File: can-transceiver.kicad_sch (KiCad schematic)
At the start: 4 parts, among them U600 TJA1044GTK_3Z

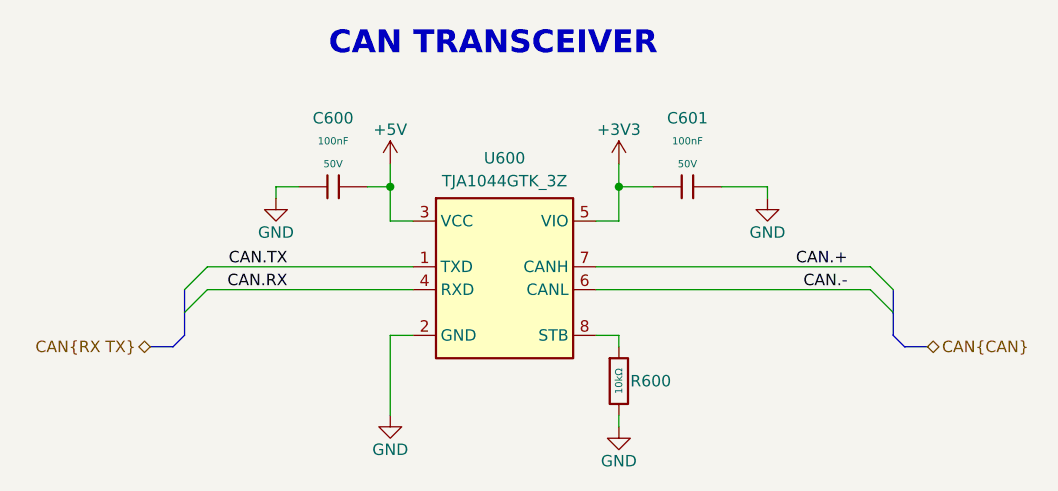
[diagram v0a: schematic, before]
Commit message: Change MCU and update library
Changed MCU from H7 to H5 series due to programming issues with external
loader. Also updated JLCPCB components (not all tho there are still
arround 18 components to fix)
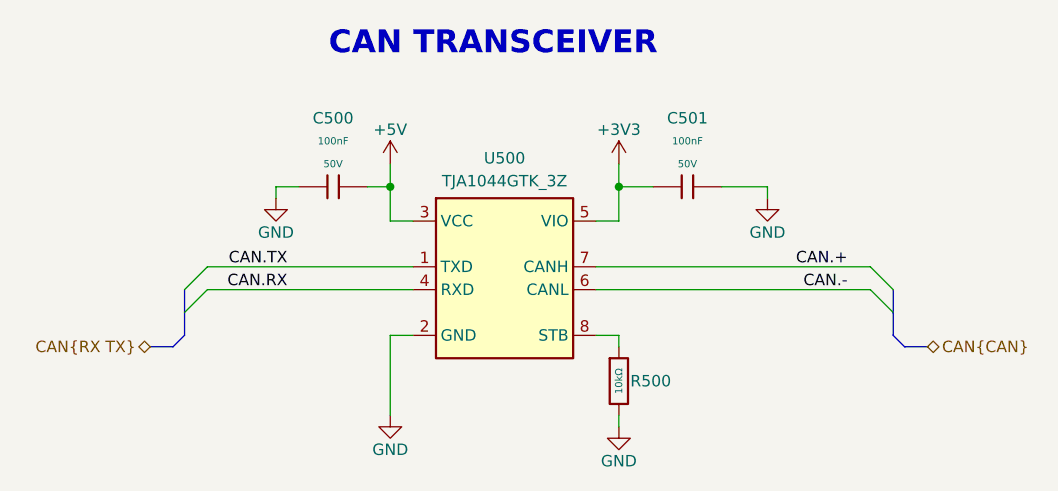
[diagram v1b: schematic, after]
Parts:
- C500: renamed from C600; Stock 3851753 -> 5436546
- C501: renamed from C601; Stock 3851753 -> 5436546
- R500: renamed from R600; Stock 14017682 -> 13746052
- renumbered U600 to U500
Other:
- title: ModuCard base module -> ModuCard BM STM32H562VGT6
